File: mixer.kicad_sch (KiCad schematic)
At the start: 6 parts, among them J4 Conn_01x03_Male, U3 TL072

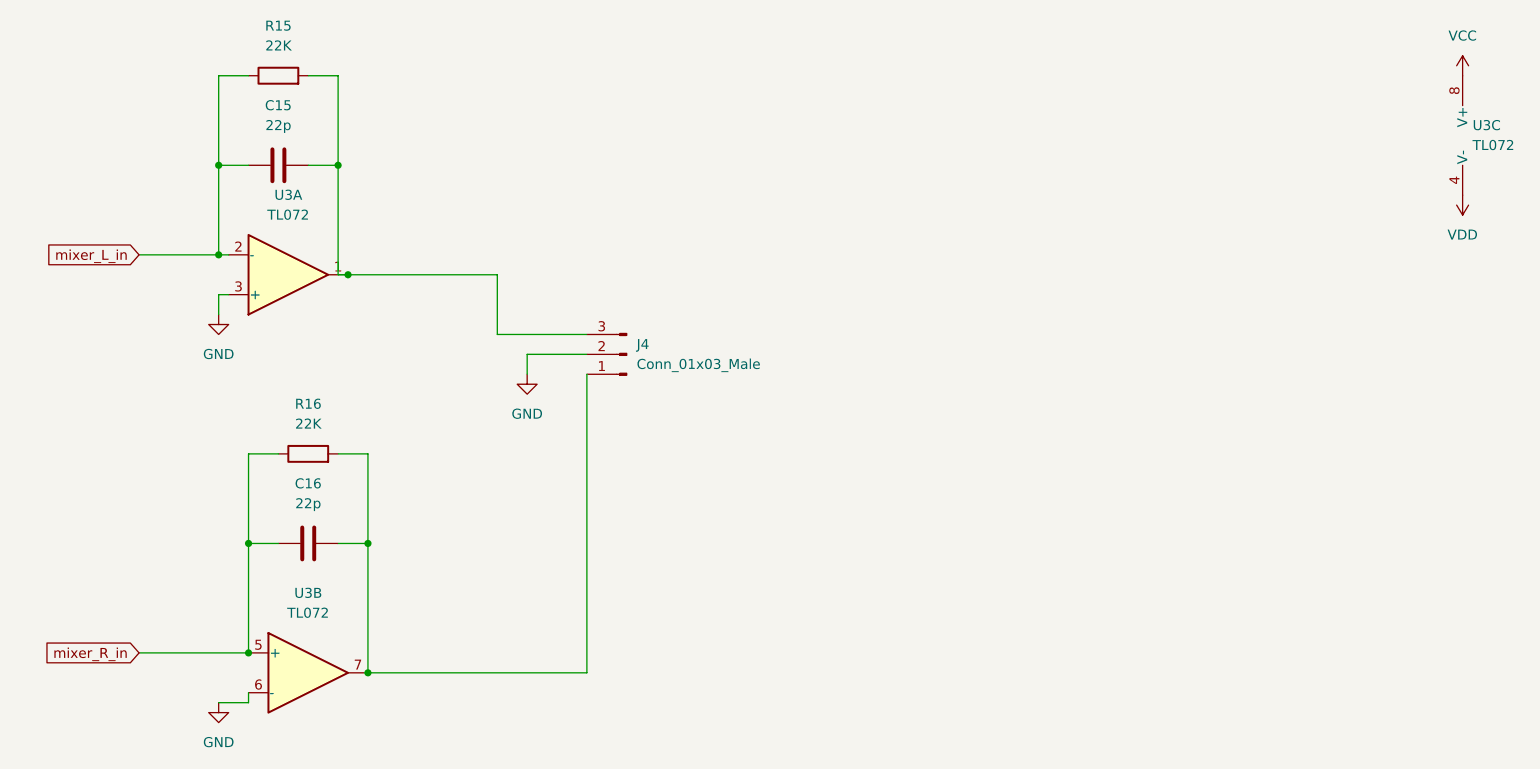
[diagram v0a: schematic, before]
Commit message: Added decoupling and output caps
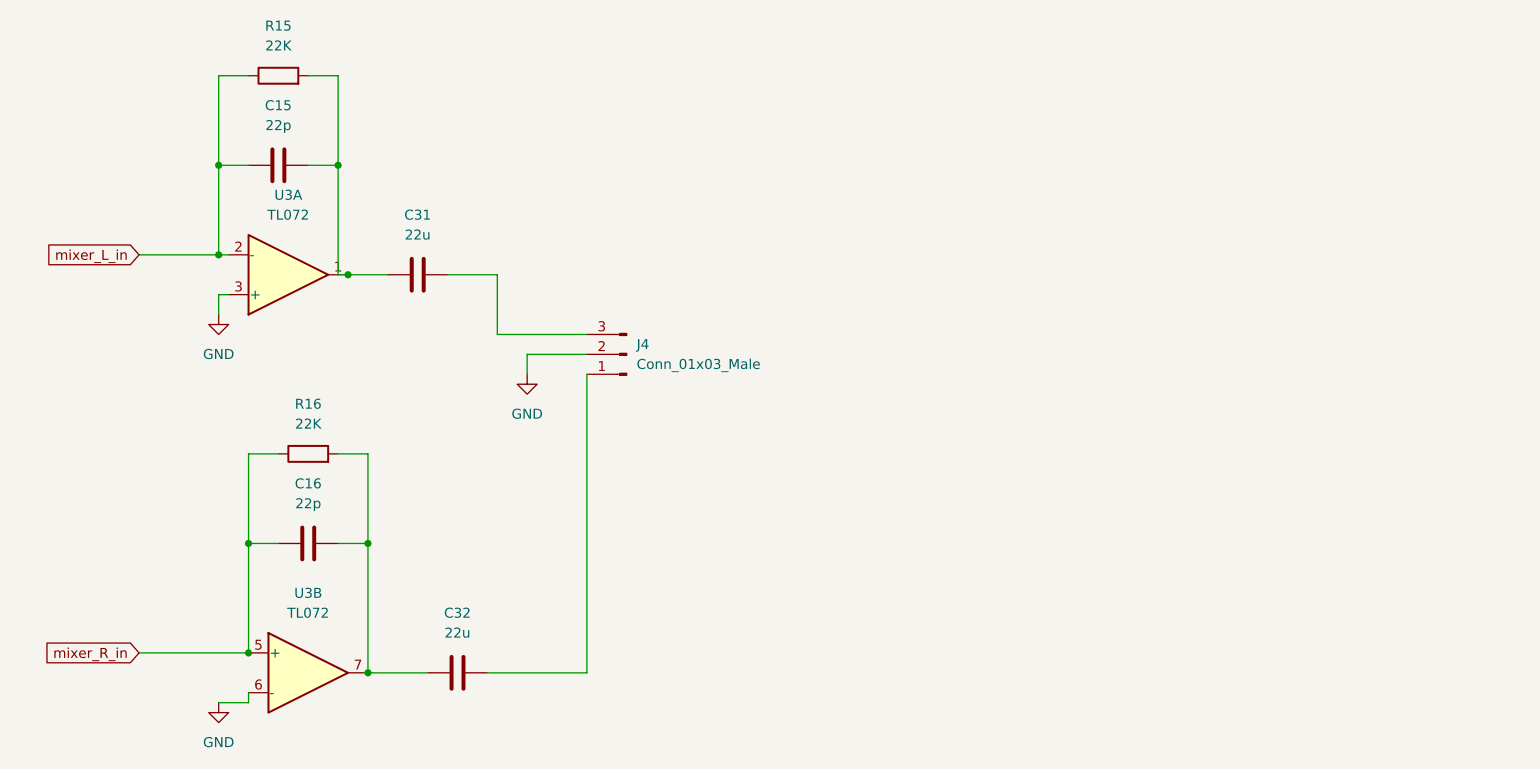
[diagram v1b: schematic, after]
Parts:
- removed unit 3 of U3
- added C31, C32: 22u, symbol Device:C
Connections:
- net at C16.2, R16.2, U3.7: now also C32.1; no longer J4.1 (Pin_1)
- net at C15.2, R15.2, U3.1: now also C31.1; no longer J4.3 (Pin_3)
- new net: C32.2, J4.1 (Pin_1)
- new net: C31.2, J4.3 (Pin_3)
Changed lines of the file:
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@@
+    (stroke (width 0) (type default) (color 0 0 0 0))
+  )
+  (wire (pts (xy 129.54 54.61) (xy 135.89 54.61))
     (stroke (width 0) (type default) (color 0 0 0 0))
   )
@@
     (stroke (width 0) (type default) (color 0 0 0 0))
   )
+  (wire (pts (xy 119.38 105.41) (xy 127 105.41))
+    (stroke (width 0) (type default) (color 0 0 0 0))
+  )
   (wire (pts (xy 119.38 88.9) (xy 119.38 105.41))
     (stroke (width 0) (type default) (color 0 0 0 0))
@@
     (stroke (width 0) (type default) (color 0 0 0 0))
   )
-  (wire (pts (xy 119.38 105.41) (xy 147.32 105.41))
-    (stroke (width 0) (type default) (color 0 0 0 0))
-  )
   (wire (pts (xy 115.57 77.47) (xy 119.38 77.47))
     (stroke (width 0) (type default) (color 0 0 0 0))
@@
     (stroke (width 0) (type default) (color 0 0 0 0))
   )
-  (wire (pts (xy 116.84 54.61) (xy 135.89 54.61))
-    (stroke (width 0) (type default) (color 0 0 0 0))
-  )
   (wire (pts (xy 115.57 54.61) (xy 116.84 54.61))
     (stroke (width 0) (type default) (color 0 0 0 0))
@@
     (stroke (width 0) (type default) (color 0 0 0 0))
   )
+  (wire (pts (xy 116.84 54.61) (xy 121.92 54.61))
+    (stroke (width 0) (type default) (color 0 0 0 0))
+  )
   (wire (pts (xy 104.14 40.64) (xy 100.33 40.64))
     (stroke (width 0) (type default) (color 0 0 0 0))
@@
   )
   (wire (pts (xy 139.7 64.77) (xy 139.7 67.31))
+    (stroke (width 0) (type default) (color 0 0 0 0))
+  )
+  (wire (pts (xy 134.62 105.41) (xy 147.32 105.41))
     (stroke (width 0) (type default) (color 0 0 0 0))
   )
@@
     (pin "8")
   )
-  (symbol (lib_id "power:VDD") (at 259.08 44.45 0) (mirror x) (unit 1)
-    (in_bom yes) (on_board yes) (fields_autoplaced)
-    (property "Reference" "#PWR0111" (id 0) (at 259.08 40.64 0)
-      (effects (font (size 1.27 1.27)) hide)
-    )
-    (property "Value" "VDD" (id 1) (at 259.08 49.53 0))
-    (property "Footprint" "" (id 2) (at 259.08 44.45 0)
-      (effects (font (size 1.27 1.27)) hide)
-    )
-    (property "Datasheet" "" (id 3) (at 259.08 44.45 0)
-      (effects (font (size 1.27 1.27)) hide)
-    )
-    (pin "1")
-  )
   (symbol (lib_id "power:GND") (at 100.33 109.22 0) (unit 1)
     (in_bom yes) (on_board yes) (fields_autoplaced)
@@
     (pin "2")
   )
-  (symbol (lib_id "power:VCC") (at 259.08 29.21 0) (unit 1)
-    (in_bom yes) (on_board yes) (fields_autoplaced)
-    (property "Reference" "#PWR0112" (id 0) (at 259.08 33.02 0)
-      (effects (font (size 1.27 1.27)) hide)
-    )
-    (property "Value" "VCC" (id 1) (at 259.08 24.13 0))
-    (property "Footprint" "" (id 2) (at 259.08 29.21 0)
-      (effects (font (size 1.27 1.27)) hide)
-    )
-    (property "Datasheet" "" (id 3) (at 259.08 29.21 0)
-      (effects (font (size 1.27 1.27)) hide)
-    )
-    (pin "1")
-  )
   (symbol (lib_id "Device:R") (at 107.95 29.21 90) (unit 1)
     (in_bom yes) (on_board yes) (fields_autoplaced)
@@
     (pin "2")
   )
-  (symbol (lib_id "Amplifier_Operational:TL072") (at 261.62 36.83 0) (unit 3)
-    (in_bom yes) (on_board yes) (fields_autoplaced)
-    (property "Reference" "U3" (id 0) (at 260.35 35.5599 0)
-      (effects (font (size 1.27 1.27)) (justify left))
-    )
-    (property "Value" "TL072" (id 1) (at 260.35 38.0999 0)
-      (effects (font (size 1.27 1.27)) (justify left))
-    )
-    (property "Footprint" "" (id 2) (at 261.62 36.83 0)
-      (effects (font (size 1.27 1.27)) hide)
-    )
-    (property "Datasheet" "http://www.ti.com/lit/ds/symlink/tl071.pdf" (id 3) (at 261.62 36.83 0)
-      (effects (font (size 1.27 1.27)) hide)
-    )
-    (pin "1")
-    (pin "2")
-    (pin "3")
-    (pin "5")
-    (pin "6")
-    (pin "7")
-    (pin "4")
-    (pin "8")
+  (symbol (lib_id "Device:C") (at 130.81 105.41 90) (unit 1)
+    (in_bom yes) (on_board yes) (fields_autoplaced)
+    (property "Reference" "C32" (id 0) (at 130.81 97.79 90))
+    (property "Value" "22u" (id 1) (at 130.81 100.33 90))
+    (property "Footprint" "" (id 2) (at 134.62 104.4448 0)
+      (effects (font (size 1.27 1.27)) hide)
+    )
+    (property "Datasheet" "~" (id 3) (at 130.81 105.41 0)
+      (effects (font (size 1.27 1.27)) hide)
+    )
+    (pin "1")
+    (pin "2")
   )
   (symbol (lib_id "Connector:Conn_01x03_Male") (at 152.4 64.77 180) (unit 1)
@@
     (pin "3")
   )
+  (symbol (lib_id "Device:C") (at 125.73 54.61 90) (unit 1)
+    (in_bom yes) (on_board yes) (fields_autoplaced)
+    (property "Reference" "C31" (id 0) (at 125.73 46.99 90))
+    (property "Value" "22u" (id 1) (at 125.73 49.53 90))
+    (property "Footprint" "" (id 2) (at 129.54 53.6448 0)
+      (effects (font (size 1.27 1.27)) hide)
+    )
+    (property "Datasheet" "~" (id 3) (at 125.73 54.61 0)
+      (effects (font (size 1.27 1.27)) hide)
+    )
+    (pin "1")
+    (pin "2")
+  )
 )

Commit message: Refactored and made modular inputs
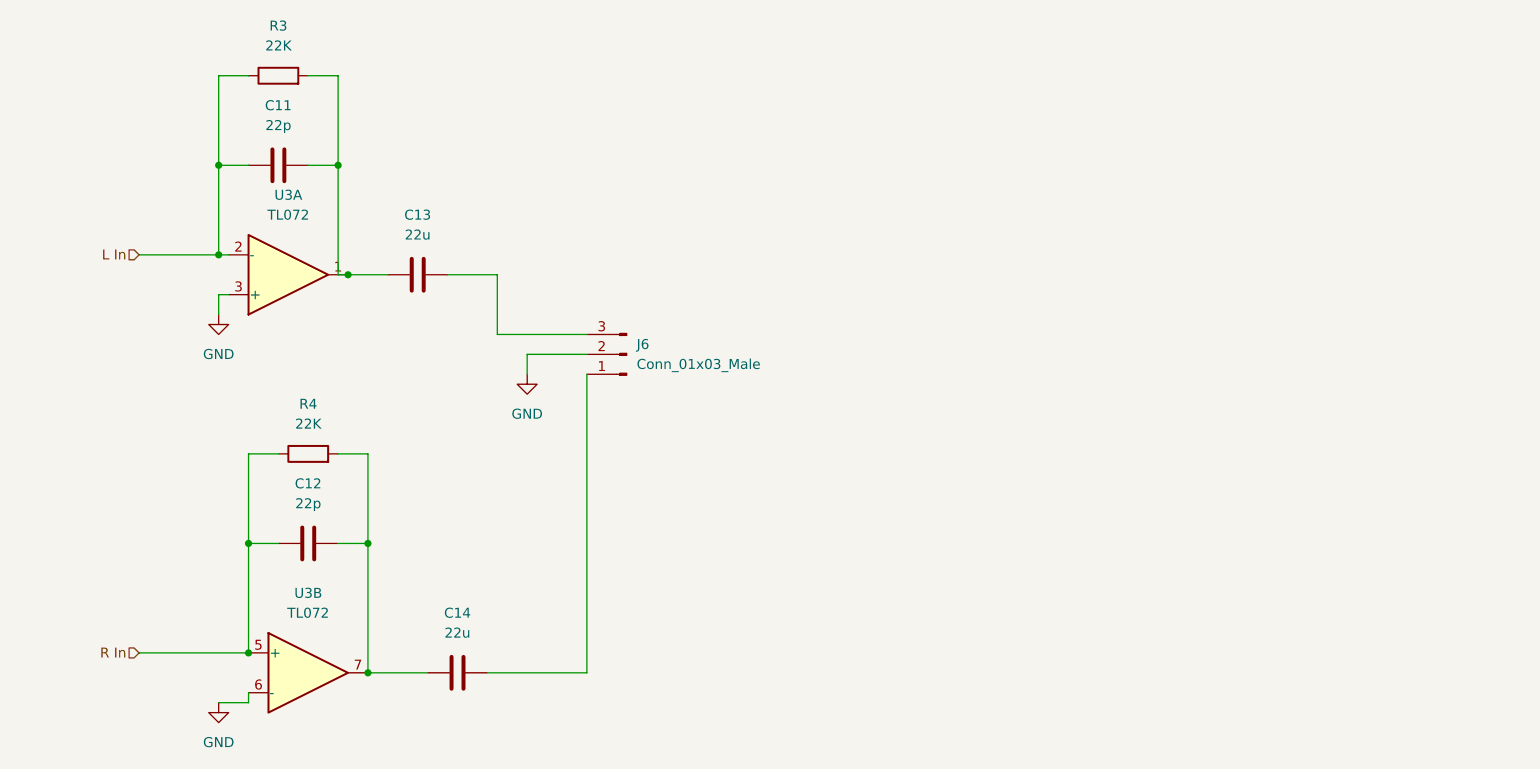
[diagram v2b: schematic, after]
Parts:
- J6: renamed from J4; footprint (none) -> Connector_JST:JST_EH_B3B-EH-A_1x03_P2.50mm_Vertical
- renumbered C15 to C11, C16 to C12, C31 to C13, C32 to C14, R15 to R3, R16 to R4
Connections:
- net mixer_L_in renamed L In
- net mixer_R_in renamed R In
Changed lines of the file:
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@@
     (stroke (width 0) (type default) (color 0 0 0 0))
   )
-  (global_label "mixer_L_in" (shape input) (at 90.17 52.07 180) (fields_autoplaced)
+  (hierarchical_label "R In" (shape input) (at 90.17 102.87 180)
     (effects (font (size 1.27 1.27)) (justify right))
-    (property "Intersheet References" "${INTERSHEET_REFS}" (id 0) (at 77.8388 51.9906 0)
-      (effects (font (size 1.27 1.27)) (justify right) hide)
-    )
   )
-  (global_label "mixer_R_in" (shape input) (at 90.17 102.87 180) (fields_autoplaced)
+  (hierarchical_label "L In" (shape input) (at 90.17 52.07 180)
     (effects (font (size 1.27 1.27)) (justify right))
-    (property "Intersheet References" "${INTERSHEET_REFS}" (id 0) (at 77.5969 102.7906 0)
-      (effects (font (size 1.27 1.27)) (justify right) hide)
-    )
   )
   (symbol (lib_id "power:GND") (at 100.33 59.69 0) (unit 1)
     (in_bom yes) (on_board yes) (fields_autoplaced)
-    (property "Reference" "#PWR0113" (id 0) (at 100.33 66.04 0)
+    (property "Reference" "#PWR017" (id 0) (at 100.33 66.04 0)
       (effects (font (size 1.27 1.27)) hide)
     )
@@
   (symbol (lib_id "Device:C") (at 111.76 88.9 90) (unit 1)
     (in_bom yes) (on_board yes) (fields_autoplaced)
-    (property "Reference" "C16" (id 0) (at 111.76 81.28 90))
+    (property "Reference" "C12" (id 0) (at 111.76 81.28 90))
     (property "Value" "22p" (id 1) (at 111.76 83.82 90))
     (property "Footprint" "" (id 2) (at 115.57 87.9348 0)
@@
   (symbol (lib_id "power:GND") (at 139.7 67.31 0) (unit 1)
     (in_bom yes) (on_board yes) (fields_autoplaced)
-    (property "Reference" "#PWR0115" (id 0) (at 139.7 73.66 0)
+    (property "Reference" "#PWR019" (id 0) (at 139.7 73.66 0)
       (effects (font (size 1.27 1.27)) hide)
     )
@@
   (symbol (lib_id "Device:C") (at 107.95 40.64 90) (unit 1)
     (in_bom yes) (on_board yes) (fields_autoplaced)
-    (property "Reference" "C15" (id 0) (at 107.95 33.02 90))
+    (property "Reference" "C11" (id 0) (at 107.95 33.02 90))
     (property "Value" "22p" (id 1) (at 107.95 35.56 90))
     (property "Footprint" "" (id 2) (at 111.76 39.6748 0)
@@
   (symbol (lib_id "power:GND") (at 100.33 109.22 0) (unit 1)
     (in_bom yes) (on_board yes) (fields_autoplaced)
-    (property "Reference" "#PWR0114" (id 0) (at 100.33 115.57 0)
+    (property "Reference" "#PWR018" (id 0) (at 100.33 115.57 0)
       (effects (font (size 1.27 1.27)) hide)
     )
@@
   (symbol (lib_id "Device:R") (at 111.76 77.47 90) (unit 1)
     (in_bom yes) (on_board yes) (fields_autoplaced)
-    (property "Reference" "R16" (id 0) (at 111.76 71.12 90))
+    (property "Reference" "R4" (id 0) (at 111.76 71.12 90))
     (property "Value" "22K" (id 1) (at 111.76 73.66 90))
     (property "Footprint" "" (id 2) (at 111.76 79.248 90)
@@
   (symbol (lib_id "Device:R") (at 107.95 29.21 90) (unit 1)
     (in_bom yes) (on_board yes) (fields_autoplaced)
-    (property "Reference" "R15" (id 0) (at 107.95 22.86 90))
+    (property "Reference" "R3" (id 0) (at 107.95 22.86 90))
     (property "Value" "22K" (id 1) (at 107.95 25.4 90))
     (property "Footprint" "" (id 2) (at 107.95 30.988 90)
@@
   (symbol (lib_id "Device:C") (at 130.81 105.41 90) (unit 1)
     (in_bom yes) (on_board yes) (fields_autoplaced)
-    (property "Reference" "C32" (id 0) (at 130.81 97.79 90))
+    (property "Reference" "C14" (id 0) (at 130.81 97.79 90))
     (property "Value" "22u" (id 1) (at 130.81 100.33 90))
     (property "Footprint" "" (id 2) (at 134.62 104.4448 0)
@@
   (symbol (lib_id "Connector:Conn_01x03_Male") (at 152.4 64.77 180) (unit 1)
     (in_bom yes) (on_board yes) (fields_autoplaced)
-    (property "Reference" "J4" (id 0) (at 153.67 63.4999 0)
+    (property "Reference" "J6" (id 0) (at 153.67 63.4999 0)
       (effects (font (size 1.27 1.27)) (justify right))
     )
@@
       (effects (font (size 1.27 1.27)) (justify right))
     )
-    (property "Footprint" "" (id 2) (at 152.4 64.77 0)
+    (property "Footprint" "Connector_JST:JST_EH_B3B-EH-A_1x03_P2.50mm_Vertical" (id 2) (at 152.4 64.77 0)
       (effects (font (size 1.27 1.27)) hide)
     )
@@
   (symbol (lib_id "Device:C") (at 125.73 54.61 90) (unit 1)
     (in_bom yes) (on_board yes) (fields_autoplaced)
-    (property "Reference" "C31" (id 0) (at 125.73 46.99 90))
+    (property "Reference" "C13" (id 0) (at 125.73 46.99 90))
     (property "Value" "22u" (id 1) (at 125.73 49.53 90))
     (property "Footprint" "" (id 2) (at 129.54 53.6448 0)

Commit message: Update footprints
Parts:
- C13, C14: footprint (none) -> Capacitor_THT:C_Radial_D6.3mm_H11.0mm_P2.50mm
- U3: footprint (none) -> Package_DIP:DIP-8_W7.62mm_Socket
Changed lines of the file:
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@@
     (property "Reference" "U3" (id 0) (at 109.22 44.45 0))
     (property "Value" "TL072" (id 1) (at 109.22 46.99 0))
-    (property "Footprint" "" (id 2) (at 109.22 54.61 0)
+    (property "Footprint" "Package_DIP:DIP-8_W7.62mm_Socket" (id 2) (at 109.22 54.61 0)
       (effects (font (size 1.27 1.27)) hide)
     )
@@
     (property "Reference" "U3" (id 0) (at 111.76 95.25 0))
     (property "Value" "TL072" (id 1) (at 111.76 97.79 0))
-    (property "Footprint" "" (id 2) (at 111.76 105.41 0)
+    (property "Footprint" "Package_DIP:DIP-8_W7.62mm_Socket" (id 2) (at 111.76 105.41 0)
       (effects (font (size 1.27 1.27)) hide)
     )
@@
     (property "Reference" "C14" (id 0) (at 130.81 97.79 90))
     (property "Value" "22u" (id 1) (at 130.81 100.33 90))
-    (property "Footprint" "" (id 2) (at 134.62 104.4448 0)
+    (property "Footprint" "Capacitor_THT:C_Radial_D6.3mm_H11.0mm_P2.50mm" (id 2) (at 134.62 104.4448 0)
       (effects (font (size 1.27 1.27)) hide)
     )
@@
     (property "Reference" "C13" (id 0) (at 125.73 46.99 90))
     (property "Value" "22u" (id 1) (at 125.73 49.53 90))
-    (property "Footprint" "" (id 2) (at 129.54 53.6448 0)
+    (property "Footprint" "Capacitor_THT:C_Radial_D6.3mm_H11.0mm_P2.50mm" (id 2) (at 129.54 53.6448 0)
       (effects (font (size 1.27 1.27)) hide)
     )

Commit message: Finalize schematic and start with PCB layout
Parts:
- C11, C12: footprint (none) -> Capacitor_THT:C_Disc_D5.1mm_W3.2mm_P5.00mm
- R3, R4: footprint (none) -> Resistor_THT:R_Axial_DIN0207_L6.3mm_D2.5mm_P10.16mm_Horizontal
- renumbered U3 to U1
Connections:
- net GND: no longer J6.2 (Pin_2)
- new net VDD: J6.2 (Pin_2)
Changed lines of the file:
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@@
     (effects (font (size 1.27 1.27)) (justify right))
+  )
+  (symbol (lib_id "power:VDD") (at 139.7 67.31 180) (unit 1)
+    (in_bom yes) (on_board yes) (fields_autoplaced)
+    (property "Reference" "#PWR019" (id 0) (at 139.7 63.5 0)
+      (effects (font (size 1.27 1.27)) hide)
+    )
+    (property "Value" "VDD" (id 1) (at 139.7 72.39 0))
+    (property "Footprint" "" (id 2) (at 139.7 67.31 0)
+      (effects (font (size 1.27 1.27)) hide)
+    )
+    (property "Datasheet" "" (id 3) (at 139.7 67.31 0)
+      (effects (font (size 1.27 1.27)) hide)
+    )
+    (pin "1")
   )
   (symbol (lib_id "power:GND") (at 100.33 59.69 0) (unit 1)
@@
     (property "Reference" "C12" (id 0) (at 111.76 81.28 90))
     (property "Value" "22p" (id 1) (at 111.76 83.82 90))
-    (property "Footprint" "" (id 2) (at 115.57 87.9348 0)
+    (property "Footprint" "Capacitor_THT:C_Disc_D5.1mm_W3.2mm_P5.00mm" (id 2) (at 115.57 87.9348 0)
       (effects (font (size 1.27 1.27)) hide)
     )
@@
     (pin "2")
   )
-  (symbol (lib_id "power:GND") (at 139.7 67.31 0) (unit 1)
-    (in_bom yes) (on_board yes) (fields_autoplaced)
-    (property "Reference" "#PWR019" (id 0) (at 139.7 73.66 0)
-      (effects (font (size 1.27 1.27)) hide)
-    )
-    (property "Value" "GND" (id 1) (at 139.7 72.39 0))
-    (property "Footprint" "" (id 2) (at 139.7 67.31 0)
-      (effects (font (size 1.27 1.27)) hide)
-    )
-    (property "Datasheet" "" (id 3) (at 139.7 67.31 0)
-      (effects (font (size 1.27 1.27)) hide)
-    )
-    (pin "1")
-  )
   (symbol (lib_id "Device:C") (at 107.95 40.64 90) (unit 1)
     (in_bom yes) (on_board yes) (fields_autoplaced)
     (property "Reference" "C11" (id 0) (at 107.95 33.02 90))
     (property "Value" "22p" (id 1) (at 107.95 35.56 90))
-    (property "Footprint" "" (id 2) (at 111.76 39.6748 0)
+    (property "Footprint" "Capacitor_THT:C_Disc_D5.1mm_W3.2mm_P5.00mm" (id 2) (at 111.76 39.6748 0)
       (effects (font (size 1.27 1.27)) hide)
     )
@@
   (symbol (lib_id "Amplifier_Operational:TL072") (at 109.22 54.61 0) (mirror x) (unit 1)
     (in_bom yes) (on_board yes) (fields_autoplaced)
-    (property "Reference" "U3" (id 0) (at 109.22 44.45 0))
+    (property "Reference" "U1" (id 0) (at 109.22 44.45 0))
     (property "Value" "TL072" (id 1) (at 109.22 46.99 0))
     (property "Footprint" "Package_DIP:DIP-8_W7.62mm_Socket" (id 2) (at 109.22 54.61 0)
@@
   (symbol (lib_id "Amplifier_Operational:TL072") (at 111.76 105.41 0) (unit 2)
     (in_bom yes) (on_board yes) (fields_autoplaced)
-    (property "Reference" "U3" (id 0) (at 111.76 95.25 0))
+    (property "Reference" "U1" (id 0) (at 111.76 95.25 0))
     (property "Value" "TL072" (id 1) (at 111.76 97.79 0))
     (property "Footprint" "Package_DIP:DIP-8_W7.62mm_Socket" (id 2) (at 111.76 105.41 0)
@@
     (property "Reference" "R4" (id 0) (at 111.76 71.12 90))
     (property "Value" "22K" (id 1) (at 111.76 73.66 90))
-    (property "Footprint" "" (id 2) (at 111.76 79.248 90)
+    (property "Footprint" "Resistor_THT:R_Axial_DIN0207_L6.3mm_D2.5mm_P10.16mm_Horizontal" (id 2) (at 111.76 79.248 90)
       (effects (font (size 1.27 1.27)) hide)
     )
@@
     (property "Reference" "R3" (id 0) (at 107.95 22.86 90))
     (property "Value" "22K" (id 1) (at 107.95 25.4 90))
-    (property "Footprint" "" (id 2) (at 107.95 30.988 90)
+    (property "Footprint" "Resistor_THT:R_Axial_DIN0207_L6.3mm_D2.5mm_P10.16mm_Horizontal" (id 2) (at 107.95 30.988 90)
       (effects (font (size 1.27 1.27)) hide)
     )
